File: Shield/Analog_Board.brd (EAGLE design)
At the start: 101.6 x 53.3 mm, 62 parts, among them IC1 INA105U, IC2 ACPL-C87A-000E, IC3 ACPL-C87A-000E, IC4 INA105U, IC5 ACPL-C87A-000E, IC6 INA105U, IC7 ACPL-C87A-000E, IC8 INA105U

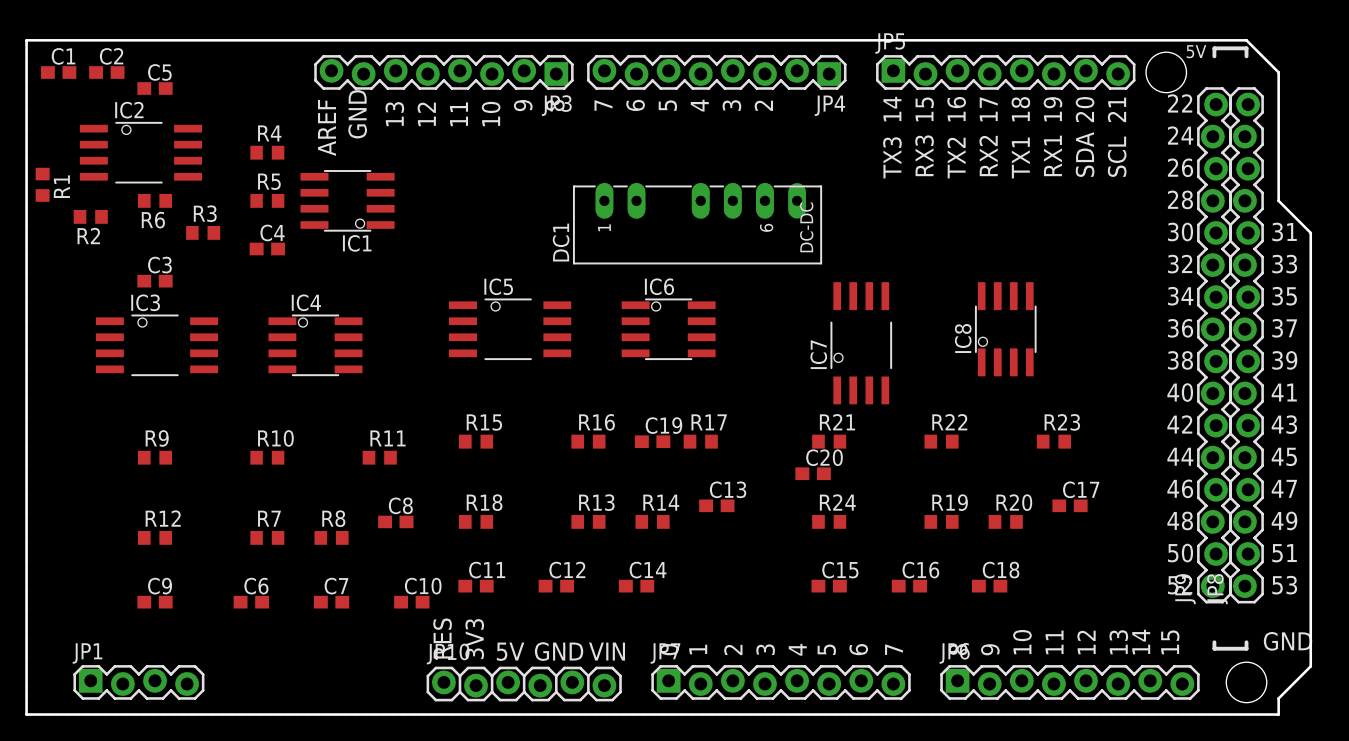
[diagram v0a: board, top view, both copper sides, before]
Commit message: Newer version of analog board, new version of DueD
Dued board now properly sized for the new case.
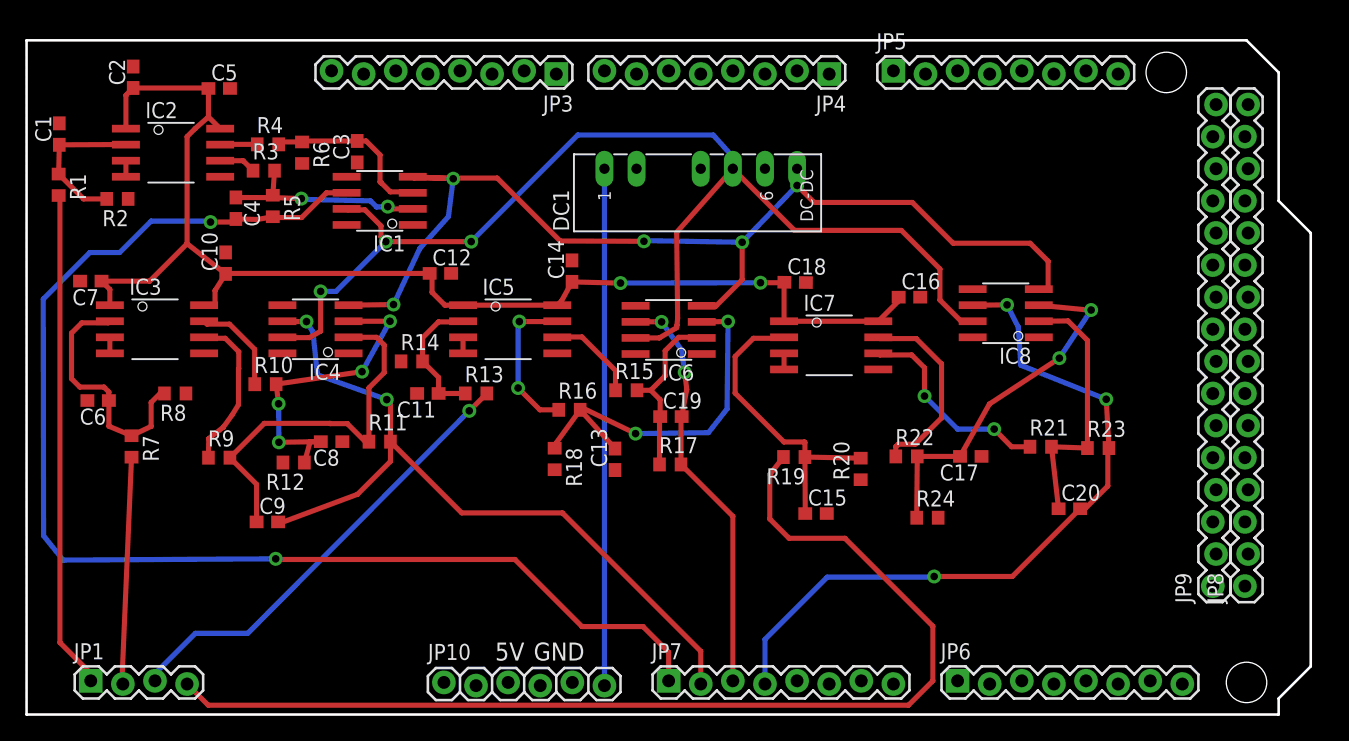
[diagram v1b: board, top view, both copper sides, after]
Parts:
- moved C7 31.8 mm to (5.08, 34.3), turned to 180 degrees
- moved C10 30.6 mm to (15.7, 35.7), turned to 90 degrees
- moved C18 28.5 mm to (60.8, 34.2), turned to 359.3 degrees
- moved C12 26.4 mm to (32.7, 34.9)
- moved C14 25.4 mm to (43.2, 35.1), turned to 90 degrees
- moved R14 22.9 mm to (30.5, 27.9)
- moved C16 22.9 mm to (69.8, 33.0)
- moved C20 20.5 mm to (82.5, 16.3)
- moved C6 20.0 mm to (5.66, 24.8), turned to 180 degrees
- moved C3 19.0 mm to (26.2, 44.5), turned to 90 degrees
- moved R8 16.8 mm to (11.8, 25.4), turned to 180 degrees
- moved R21 16.7 mm to (80.2, 21.2)
- moved C11 15.7 mm to (31.8, 25.4), turned to 180 degrees
- moved R13 13.5 mm to (35.6, 25.4)
- moved R7 13.0 mm to (8.31, 21.2), turned to 270 degrees
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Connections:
- net -VOUT: now also DC1.7
- net AIN1: no longer R19.2
- net AIN4: now also R19.2
- net N$14: now also IC4.3
- net N$22: now also IC6.3
- net N$30: now also IC8.3
- net N$9: now also IC1.3
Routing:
- net A0: track 0.13 -> 102.1 mm, vias 0 -> 2
- net +5V: track 0.00 -> 101.0 mm, vias 0 -> 2
- net +VOUT: track 0.00 -> 93.0 mm, vias 0 -> 3
- net AIN4: track 0.00 -> 86.5 mm
- net -VOUT: track 0.00 -> 84.8 mm, vias 0 -> 5
- net A1: track 0.25 -> 61.5 mm, vias 0 -> 2
- net A3: track 0.13 -> 57.6 mm, vias 0 -> 3
- net VIN: track 0.25 -> 40.9 mm
- net AIN1: track 0.00 -> 39.4 mm
- net AIN3: track 0.00 -> 36.0 mm, vias 0 -> 1
- net A2: track 0.13 -> 32.9 mm, vias 0 -> 2
- net N$13: track 0.00 -> 29.9 mm
- net N$22: track 0.00 -> 29.8 mm, vias 0 -> 2
- net N$30: track 0.00 -> 28.4 mm, vias 0 -> 2
- net N$14: track 0.00 -> 25.2 mm, vias 0 -> 4
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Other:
- board text removed: "0"
- board text removed: "1"
- board text removed: "10"
- board text removed: "11"
- board text removed: "12"
- board text removed: "13"
- board text removed: "14"
- board text removed: "15"
- board text removed: "16"
- board text removed: "17"
- board text removed: "18"
- board text removed: "19"
- board text removed: "2"
- board text removed: "20"
- board text removed: "21"
- board text removed: "22"
- board text removed: "24"
- board text removed: "26"
- board text removed: "28"
- board text removed: "3"
- board text removed: "30"
- board text removed: "31"
- board text removed: "32"
- board text removed: "33"
- board text removed: "34"
- board text removed: "35"
- board text removed: "36"
- board text removed: "37"
- board text removed: "38"
- board text removed: "39"
- board text removed: "3V3"
- board text removed: "4"
- board text removed: "40"
- board text removed: "41"
- board text removed: "42"
- board text removed: "43"
- board text removed: "44"
- board text removed: "45"
- board text removed: "46"
- board text removed: "47"
- board text removed: "48"
- board text removed: "49"
- board text removed: "5"
- board text removed: "50"
- board text removed: "51"
- board text removed: "52"
- board text removed: "53"
- board text removed: "6"
- board text removed: "7"
- board text removed: "8"
- board text removed: "9"
- board text removed: "AREF"
- board text removed: "RES"
- board text removed: "RX1"
- board text removed: "RX2"
- board text removed: "RX3"
- board text removed: "SCL"
- board text removed: "SDA"
- board text removed: "TX1"
- board text removed: "TX2"
- board text removed: "TX3"
- board text removed: "VIN"
